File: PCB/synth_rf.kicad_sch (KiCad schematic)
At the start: 60 parts, among them J2 SMA CLK0, J3 SMA CLK1, J4 SMA CLK2, U2 Si5351A-B-GT, X1 25MHz TCXO

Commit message: Schematic: US resistor symbols, decoupling caps at their ICs, drop finalized VERIFY notes
- Device:R_Small -> Device:R_Small_US on all 30 resistors (same pin geometry; refs/values/fields/footprints/LCSC unchanged)
- Move label-connected decoupling caps next to their ICs: C10/C11 + C12/C13 at U3, C15/C16 at U4, C4 at U2
- Add PCB placement notes by U1, U5, U3, U4, U2/X1 and DS1 (pins from netlist)
- Remove VERIFY note lines and VERIFY fields for items Jason finalized:
  J1 D1 C10 U3 FB2 DS1 C17 SW1 X1 C100 R101 L1 C105
- Netlist identical to 4963a6d; ERC 0 errors
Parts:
- C100: VERIFY DC-block LF corner ~32 kHz into 50 ohm (PLAN Q6). -> (none)
- C105: VERIFY 9.1p only +/-0.25pF in stock (C513588); 24p +/-2% stock thi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 -> (none)
- L1: VERIFY LQW2UAS stock 0.9-3.3k/part; buy ahead. 150n uses +/-1% C20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 -> (none)
- R100, R120, R121, R140, R141, R27, R28, R5, R6: symbol Device:R_Small -> Device:R_Small_US
- R101: symbol Device:R_Small -> Device:R_Small_US; VERIFY DNP shunt ~120 ohm back-match of ~85 ohm source (datasheet 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 -> (none)
- X1: VERIFY TCXO stock thin (718); buy before ordering. -> (none)
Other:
- note added: "PCB: C4 100n at U2 pins 1 (VDD) + 7 (VDDO), tight loop to pin 8 (GND); GND via at cap pad. C5 100n at X1 pin 4 (VDD)."
- note added: "VERIFY (unconfirmed items on this sheet): - R27: I2C pull-up value not fixed (PLAN 2.2-4.7k); no LCSC chosen. On +3V3D: ATtiny, Si5351, CP2102N and OLED all at 3.3 V, so I2C levels match. - R28: as R27 - R100: 0603 0R series (Jason decision); LCSC code not in PLAN (C17477 is 0805). - J2: Footprint is a placeholder; check BWSMA-KE-P001 launch geometry and 1.6 mm edge fit. - R120: see R100 - R121: 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"
- note removed: "VERIFY (unconfirmed items on this sheet): - X1: TCXO stock thin (718); buy before ordering. - R27: I2C pull-up value not fixed (PLAN 2.2-4.7k); no LCSC chosen. On +3V3D: ATtiny, Si5351, CP2102N and OLED all at 3.3 V, so I2C levels match. - R28: as R27 - R100: 0603 0R series (Jason decision); LCSC code not in PLAN (C17477 is 0805). - C100: DC-block LF corner ~32 kHz into 50 ohm (PLAN Q6). - R101: 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"
- moved on the sheet: C4
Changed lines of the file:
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@@
 		(comment 1 "Draft schematic, not reviewed. See VERIFY notes.")
 	)
-	(text "VERIFY (unconfirmed items on this sheet):\n- X1: TCXO stock thin (718); buy before ordering.\n- R27: I2C pull-up value not fixed (PLAN 2.2-4.7k); no LCSC chosen. On +3V3D: ATtiny, Si5351, CP2102N and OLED all at\n   3.3 V, so I2C levels match.\n- R28: as R27\n- R100: 0603 0R series (Jason decision); LCSC code not in PLAN (C17477 is 0805).\n- C100: DC-block LF corner ~32 kHz into 50 ohm (PLAN Q6).\n- R101: DNP shunt ~120 ohm back-match of ~85 ohm source (datasheet Zo); part/LCSC not chosen; verify return loss esp.\n   >100 MHz.\n- L1: LQW2UAS stock 0.9-3.3k/part; buy ahead. 150n uses +/-1% C2044861 (C2043109 is +/-5%).\n- C105: 9.1p only +/-0.25pF in stock (C513588); 24p +/-2% stock thin (C2857979, ~950).\n- J2: Footprint is a placeholder; check BWSMA-KE-P001 launch geometry and 1.6 mm edge fit.\n- R120: see R100\n- R121: see R100\n- J3: see J2\n- R140: see R100\n- R141: see R100\n- J4: see J2"
+	(text "VERIFY (unconfirmed items on this sheet):\n- R27: I2C pull-up value not fixed (PLAN 2.2-4.7k); no LCSC chosen. On +3V3D: ATtiny, Si5351, CP2102N and OLED all at\n   3.3 V, so I2C levels match.\n- R28: as R27\n- R100: 0603 0R series (Jason decision); LCSC code not in PLAN (C17477 is 0805).\n- J2: Footprint is a placeholder; check BWSMA-KE-P001 launch geometry and 1.6 mm edge fit.\n- R120: see R100\n- R121: see R100\n- J3: see J2\n- R140: see R100\n- R141: see R100\n- J4: see J2"
 		(exclude_from_sim no)
 		(at 290 40 0)
@@
 		)
 	)
+	(text "PCB: C4 100n at U2 pins 1 (VDD) + 7 (VDDO), tight loop\nto pin 8 (GND); GND via at cap pad. C5 100n at X1 pin 4 (VDD)."
+		(exclude_from_sim no)
+		(at 162.56 62.23 0)
+		(effects
+			(font
+				(size 1.27 1.27)
+			)
+			(justify left top)
+		)
+	)
 	(junction
 		(at 165.1 264.16)
@@
 			)
 		)
-		(property "VERIFY" "LQW2UAS stock 0.9-3.3k/part; buy ahead. 150n uses +/-1% C2044861 (C2043109 is +/-5%)."
-			(at 121.92 172.72 0)
-			(hide yes)
-			(show_name no)
-			(do_not_autoplace no)
-			(effects
-				(font
-					(size 1.27 1.27)
-				)
-			)
-		)
 		(pin "1"
 		)
@@
 	)
 	(symbol
-		(lib_id "Device:R_Small")
+		(lib_id "Device:R_Small_US")
 		(at 139.7 129.54 0)
 		(unit 1)
@@
 	(symbol
 		(lib_id "Device:C_Small")
-		(at 165.1 59.69 0)
+		(at 154.94 76.2 0)
 		(unit 1)
 		(body_style 1)
@@
 		(dnp no)
 		(property "Reference" "C4"
-			(at 166.9 59.09 0)
+			(at 156.74 75.6 0)
 			(show_name no)
 			(do_not_autoplace no)
@@
 		)
 		(property "Value" "100n"
-			(at 166.9 61.29 0)
+			(at 156.74 77.8 0)
 			(show_name no)
 			(do_not_autoplace no)
@@
 		)
 		(property "Footprint" "Capacitor_SMD:C_0805_2012Metric"
-			(at 165.1 59.69 0)
+			(at 154.94 76.2 0)
 			(hide yes)
 			(show_name no)
@@
 		)
 		(property "Datasheet" ""
-			(at 165.1 59.69 0)
+			(at 154.94 76.2 0)
 			(hide yes)
 			(show_name no)
@@
 		)
 		(property "Description" "Unpolarized capacitor, small symbol"
-			(at 165.1 59.69 0)
+			(at 154.94 76.2 0)
 			(hide yes)
 			(show_name no)
@@
 		)
 		(property "LCSC" "C49678"
-			(at 165.1 59.69 0)
+			(at 154.94 76.2 0)
 			(hide yes)
 			(show_name no)
@@
 		)
 		(property "MPN" "CC0805KRX7R9BB104"
-			(at 165.1 59.69 0)
+			(at 154.94 76.2 0)
 			(hide yes)
 			(show_name no)
@@
 		)
 		(property "Manufacturer" "YAGEO"
-			(at 165.1 59.69 0)
+			(at 154.94 76.2 0)
 			(hide yes)
 			(show_name no)
@@
 	)
 	(symbol
-		(lib_id "Device:R_Small")
+		(lib_id "Device:R_Small_US")
 		(at 40.64 172.72 90)
 		(unit 1)
@@
 	)
 	(symbol
-		(lib_id "Device:R_Small")
+		(lib_id "Device:R_Small_US")
 		(at 40.64 264.16 90)
 		(unit 1)
@@
 			)
 		)
-		(property "VERIFY" "9.1p only +/-0.25pF in stock (C513588); 24p +/-2% stock thin (C2857979, ~950)."
-			(at 121.92 165.1 0)
-			(hide yes)
-			(show_name no)
-			(do_not_autoplace no)
-			(effects
-				(font
-					(size 1.27 1.27)
-				)
-			)
-		)
 		(pin "1"
 		)
@@
 			)
 		)
-		(property "VERIFY" "DC-block LF corner ~32 kHz into 50 ohm (PLAN Q6)."
-			(at 50.8 172.72 0)
-			(hide yes)
-			(show_name no)
-			(do_not_autoplace no)
-			(effects
-				(font
-					(size 1.27 1.27)
-				)
-			)
-		)
 		(pin "1"
 		)
@@
 	)
 	(symbol
-		(lib_id "Device:R_Small")
+		(lib_id "Device:R_Small_US")
 		(at 40.64 218.44 90)
 		(unit 1)
@@
 	)
 	(symbol
-		(lib_id "Device:R_Small")
+		(lib_id "Device:R_Small_US")
 		(at 60.96 177.8 0)
 		(unit 1)
@@
 			)
 		)
-		(property "VERIFY" "DNP shunt ~120 ohm back-match of ~85 ohm source (datasheet Zo); part/LCSC not chosen; verify return loss esp. >100 MHz."
-			(at 60.96 177.8 0)
-			(hide yes)
-			(show_name no)
-			(do_not_autoplace no)
-			(effects
-				(font
-					(size 1.27 1.27)
-				)
-			)
-		)
 		(pin "1"
 		)
@@
 	)
 	(symbol
-		(lib_id "Device:R_Small")
+		(lib_id "Device:R_Small_US")
 		(at 59.69 67.31 0)
 		(unit 1)
@@
 	)
 	(symbol
-		(lib_id "Device:R_Small")
+		(lib_id "Device:R_Small_US")
 		(at 60.96 223.52 0)
 		(unit 1)
@@
 			)
 		)
-		(property "VERIFY" "TCXO stock thin (718); buy before ordering."
-			(at 59.69 87.63 0)
-			(hide yes)
-			(show_name no)
-			(do_not_autoplace no)
-			(effects
-				(font
-					(size 1.27 1.27)
-				)
-			)
-		)
 		(pin "1"
 		)
@@
 	)
 	(symbol
-		(lib_id "Device:R_Small")
+		(lib_id "Device:R_Small_US")
 		(at 44.45 74.93 0)
 		(unit 1)
@@
 	)
 	(symbol
-		(lib_id "Device:R_Small")
+		(lib_id "Device:R_Small_US")
 		(at 100.33 129.54 0)
 		(unit 1)
@@
 	(symbol
 		(lib_id "power:GND")
-		(at 165.1 62.23 0)
+		(at 154.94 78.74 0)
 		(unit 1)
 		(body_style 1)
@@
 		(dnp no)
 		(property "Reference" "#PWR087"
-			(at 165.1 62.23 0)
+			(at 154.94 78.74 0)
 			(hide yes)
 			(show_name no)
@@
 		)
 		(property "Value" "GND"
-			(at 165.1 66.04 0)
+			(at 154.94 82.55 0)
 			(show_name no)
 			(do_not_autoplace no)
@@
 		)
 		(property "Footprint" ""
-			(at 165.1 62.23 0)
+			(at 154.94 78.74 0)
 			(hide yes)
 			(show_name no)
@@
 		)
 		(property "Datasheet" ""
-			(at 165.1 62.23 0)
+			(at 154.94 78.74 0)
 			(hide yes)
 			(show_name no)
@@
 		)
 		(property "Description" ""
-			(at 165.1 62.23 0)
+			(at 154.94 78.74 0)
 			(show_name no)
 			(do_not_autoplace no)
@@
 	)
 	(symbol
-		(lib_id "Device:R_Small")
+		(lib_id "Device:R_Small_US")
 		(at 60.96 269.24 0)
 		(unit 1)
@@
 	(symbol
 		(lib_id "power:+3V3")
-		(at 165.1 57.15 0)
+		(at 154.94 73.66 0)
 		(unit 1)
 		(body_style 1)
@@
 		(dnp no)
 		(property "Reference" "#PWR086"
-			(at 165.1 57.15 0)
+			(at 154.94 73.66 0)
 			(hide yes)
 			(show_name no)
@@
 		)
 		(property "Value" "+3V3_CLK"
-			(at 165.1 53.34 0)
+			(at 154.94 69.85 0)
 			(show_name no)
 			(do_not_autoplace no)
@@
 		)
 		(property "Footprint" ""
-			(at 165.1 57.15 0)
+			(at 154.94 73.66 0)
 			(hide yes)
 			(show_name no)
@@
 		)
 		(property "Datasheet" ""
-			(at 165.1 57.15 0)
+			(at 154.94 73.66 0)
 			(hide yes)
 			(show_name no)
@@
 		)
 		(property "Description" ""
-			(at 165.1 57.15 0)
+			(at 154.94 73.66 0)
 			(show_name no)
 			(do_not_autoplace no)

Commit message: Resolve VERIFY directives: R9 to VIO, R29 on PB4, OLED bulk, SMD UPDI parts, 4.7k I2C, 0805 0R, Etherkit SMA footprint
- R9 /RST pull-up moved from +5V to CP_VDD (CP2102N DS 2.1, Table 3.10)
- New R29 1k (C21190) between C14 and PB4 to limit DTR-rise injection current (ATtiny3226 DS Table 33-1)
- C24 fitted 22u 1206 (C12891); C22/C23 kept 2x4.7u
- R13 0603 C23179, D4 1N5711W SOD-123 C154843, J5 1x4 pin header C124378
- R27/R28 4.7k C17673; R100/R120/R140 0805 0R C17477; R101/R121/R141 LCSC C17437 (DNP)
- J2-J4 footprint EtherkitKicadLibrary:SMA-ENDLAUNCH
- H1-H4 and solder jumpers excluded from BOM
- Finalized VERIFY notes removed from sheets; VERIFY.md items ticked with KiCad EE notes
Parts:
- J2, J3, J4: footprint Connector_Coaxial:SMA_Samtec_SMA-J-P-H-ST-EM1_EdgeMount -> EtherkitKicadLibrary:SMA-ENDLAUNCH
- JP102, JP103, JP104, JP122, JP123, JP124, JP142, JP143, JP144: now left out of the parts list
- R100, R120, R140: footprint Resistor_SMD:R_0603_1608Metric -> Resistor_SMD:R_0805_2012Metric; LCSC (none) -> C17477; MPN (none) -> 0805W8F0000T5E; Manufacturer (none) -> UNI-ROYAL
- R101, R121, R141: LCSC (none) -> C17437; MPN (none) -> 0805W8F1200T5E; Manufacturer (none) -> UNI-ROYAL
- R27, R28: value VERIFY 2.2k-4.7k -> 4.7k; LCSC (none) -> C17673; MPN (none) -> 0805W8F4701T5E; Manufacturer (none) -> UNI-ROYAL
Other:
- note removed: "VERIFY (unconfirmed items on this sheet): - R27: I2C pull-up value not fixed (PLAN 2.2-4.7k); no LCSC chosen. On +3V3D: ATtiny, Si5351, CP2102N and OLED all at 3.3 V, so I2C levels match. - R28: as R27 - R100: 0603 0R series (Jason decision); LCSC code not in PLAN (C17477 is 0805). - J2: Footprint is a placeholder; check BWSMA-KE-P001 launch geometry and 1.6 mm edge fit. - R120: see R100 - R121: 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"

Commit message: Pre-layout: project-local Etherkit libs (ERC 0/0), DS1/J2-J4/X1 fit review, title block, clear finalized VERIFY fields, LPF closed
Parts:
- J2: VERIFY Footprint is a placeholder; check BWSMA-KE-P001 launch geom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 -> (none)
- J3, J4: VERIFY see J2 -> (none)
- R100: VERIFY 0603 0R series (Jason decision); LCSC code not in PLAN (C17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 -> (none)
- R120, R121, R140, R141: VERIFY see R100 -> (none)
- R27: VERIFY I2C pull-up value not fixed (PLAN 2.2-4.7k); no LCSC chosen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 -> (none)
- R28: VERIFY as R27 -> (none)
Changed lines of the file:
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@@
 		(rev "A")
 		(company "Etherkit / NT7S")
-		(comment 1 "Draft schematic, not reviewed. See VERIFY notes.")
+		(comment 1 "Draft schematic, not reviewed. Open items: docs/VERIFY.md")
 	)
 	(text "CLK0 output chain (J2)"
@@
 			)
 		)
-		(property "VERIFY" "as R27"
-			(at 139.7 129.54 0)
-			(hide yes)
-			(show_name no)
-			(do_not_autoplace no)
-			(effects
-				(font
-					(size 1.27 1.27)
-				)
-			)
-		)
 		(property "LCSC" "C17673"
 			(at 139.7 129.54 0)
@@
 			)
 		)
-		(property "VERIFY" "Footprint is a placeholder; check BWSMA-KE-P001 launch geometry and 1.6 mm edge fit."
-			(at 203.2 172.72 0)
-			(hide yes)
-			(show_name no)
-			(do_not_autoplace no)
-			(effects
-				(font
-					(size 1.27 1.27)
-				)
-			)
-		)
 		(pin "1"
 		)
@@
 			)
 		)
-		(property "VERIFY" "0603 0R series (Jason decision); LCSC code not in PLAN (C17477 is 0805)."
-			(at 40.64 172.72 0)
-			(hide yes)
-			(show_name no)
-			(do_not_autoplace no)
-			(effects
-				(font
-					(size 1.27 1.27)
-				)
-			)
-		)
 		(property "MPN" "0805W8F0000T5E"
 			(at 40.64 172.72 0)
@@
 			)
 		)
-		(property "VERIFY" "see R100"
-			(at 40.64 264.16 0)
-			(hide yes)
-			(show_name no)
-			(do_not_autoplace no)
-			(effects
-				(font
-					(size 1.27 1.27)
-				)
-			)
-		)
 		(property "MPN" "0805W8F0000T5E"
 			(at 40.64 264.16 0)
@@
 			)
 		)
-		(property "VERIFY" "see J2"
-			(at 203.2 264.16 0)
-			(hide yes)
-			(show_name no)
-			(do_not_autoplace no)
-			(effects
-				(font
-					(size 1.27 1.27)
-				)
-			)
-		)
 		(pin "1"
 		)
@@
 			)
 		)
-		(property "VERIFY" "see R100"
-			(at 40.64 218.44 0)
-			(hide yes)
-			(show_name no)
-			(do_not_autoplace no)
-			(effects
-				(font
-					(size 1.27 1.27)
-				)
-			)
-		)
 		(property "MPN" "0805W8F0000T5E"
 			(at 40.64 218.44 0)
@@
 			)
 		)
-		(property "VERIFY" "see R100"
-			(at 60.96 223.52 0)
-			(hide yes)
-			(show_name no)
-			(do_not_autoplace no)
-			(effects
-				(font
-					(size 1.27 1.27)
-				)
-			)
-		)
 		(property "LCSC" "C17437"
 			(at 60.96 223.52 0)
@@
 			)
 		)
-		(property "VERIFY" "see J2"
-			(at 203.2 218.44 0)
-			(hide yes)
-			(show_name no)
-			(do_not_autoplace no)
-			(effects
-				(font
-					(size 1.27 1.27)
-				)
-			)
-		)
 		(pin "1"
 		)
@@
 			)
 		)
-		(property "VERIFY" "I2C pull-up value not fixed (PLAN 2.2-4.7k); no LCSC chosen. On +3V3D: ATtiny, Si5351, CP2102N and OLED all at 3.3 V, so I2C levels match."
-			(at 100.33 129.54 0)
-			(hide yes)
-			(show_name no)
-			(do_not_autoplace no)
-			(effects
-				(font
-					(size 1.27 1.27)
-				)
-			)
-		)
 		(property "LCSC" "C17673"
 			(at 100.33 129.54 0)
@@
 			(at 60.96 269.24 0)
 			(hide yes)
-			(show_name no)
-			(do_not_autoplace no)
-			(effects
-				(font
-					(size 1.27 1.27)
-				)
-			)
-		)
-		(property "VERIFY" "see R100"
-			(at 60.96 269.24 0)
-			(hide yes)

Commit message: J2-J4 SMA: DNP, supplied in kit, user-soldered; off BOM/pos, LCSC cleared, MPN kept; VERIFY + regen docs
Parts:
- J2, J3, J4: LCSC C496550 -> (none); now not fitted; now left out of the parts list
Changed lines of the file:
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@@
 		(body_style 1)
 		(exclude_from_sim no)
-		(in_bom yes)
+		(in_bom no)
 		(on_board yes)
-		(in_pos_files yes)
-		(dnp no)
+		(in_pos_files no)
+		(dnp yes)
 		(property "Reference" "J2"
 			(at 203.454 169.672 0)
@@
 			)
 		)
-		(property "Description" "coaxial connector (BNC, SMA, SMB, SMC, Cinch/RCA, LEMO, ...)"
+		(property "Description" "SMA end-launch jack, edge mount. DNP, supplied in kit, user-soldered."
 			(at 203.2 172.72 0)
 			(hide yes)
@@
 			)
 		)
-		(property "LCSC" "C496550"
+		(property "LCSC" ""
 			(at 203.2 172.72 0)
 			(hide yes)
@@
 		(body_style 1)
 		(exclude_from_sim no)
-		(in_bom yes)
+		(in_bom no)
 		(on_board yes)
-		(in_pos_files yes)
-		(dnp no)
+		(in_pos_files no)
+		(dnp yes)
 		(property "Reference" "J4"
 			(at 203.454 261.112 0)
@@
 			)
 		)
-		(property "Description" "coaxial connector (BNC, SMA, SMB, SMC, Cinch/RCA, LEMO, ...)"
+		(property "Description" "SMA end-launch jack, edge mount. DNP, supplied in kit, user-soldered."
 			(at 203.2 264.16 0)
 			(hide yes)
@@
 			)
 		)
-		(property "LCSC" "C496550"
+		(property "LCSC" ""
 			(at 203.2 264.16 0)
 			(hide yes)
@@
 		(body_style 1)
 		(exclude_from_sim no)
-		(in_bom yes)
+		(in_bom no)
 		(on_board yes)
-		(in_pos_files yes)
-		(dnp no)
+		(in_pos_files no)
+		(dnp yes)
 		(property "Reference" "J3"
 			(at 203.454 215.392 0)
@@
 			)
 		)
-		(property "Description" "coaxial connector (BNC, SMA, SMB, SMC, Cinch/RCA, LEMO, ...)"
+		(property "Description" "SMA end-launch jack, edge mount. DNP, supplied in kit, user-soldered."
 			(at 203.2 218.44 0)
 			(hide yes)
@@
 			)
 		)
-		(property "LCSC" "C496550"
+		(property "LCSC" ""
 			(at 203.2 218.44 0)
 			(hide yes)

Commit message: Bypass: split each bypass jumper into two NO jumpers (JP104+JP105, JP124+JP125, JP144+JP145) with CLKn_BYP lane net, isolating the lane at both ends; regen docs
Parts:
- added JP105, JP125, JP145: NO, Jumper:SolderJumper-2_P1.3mm_Open_RoundedPad1.0x1.5mm, symbol Jumper:SolderJumper_2_Open
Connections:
- net at J2.1 (In), JP103.2 (B): now also JP105.2 (B); no longer JP104.2 (B)
- net at J4.1 (In), JP143.2 (B): now also JP145.2 (B); no longer JP144.2 (B)
- net at J3.1 (In), JP123.2 (B): now also JP125.2 (B); no longer JP124.2 (B)
- new net CLK0_BYP: JP104.2 (B), JP105.1 (A)
- new net CLK1_BYP: JP124.2 (B), JP125.1 (A)
- new net CLK2_BYP: JP144.2 (B), JP145.1 (A)

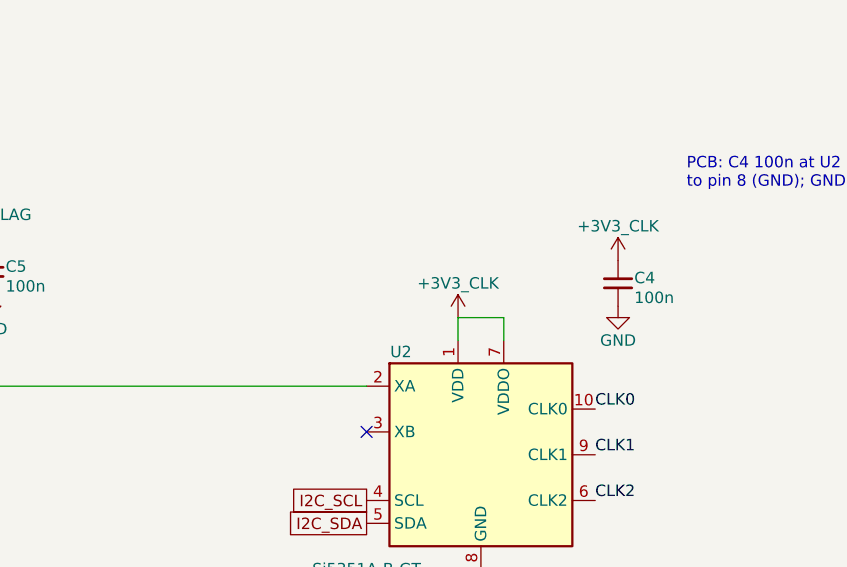
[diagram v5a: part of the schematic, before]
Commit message: Sync schematic from rev-a-schematic (24008ef): C26/C27/C28 U2 decoupling, 0402 CLK series Rs, RF50 incl. CLK*_BYP; regen docs
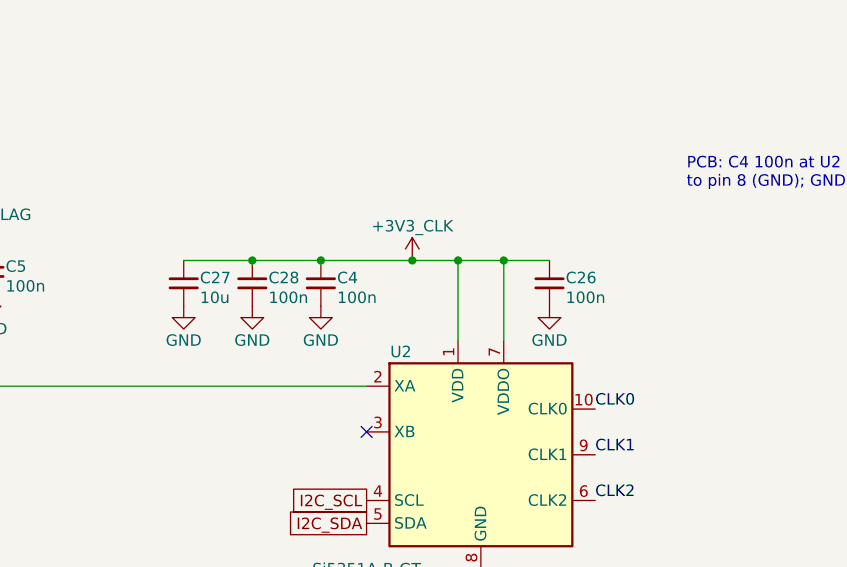
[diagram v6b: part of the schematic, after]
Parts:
- added C26: 100n, Capacitor_SMD:C_0402_1005Metric, symbol Device:C_Small
- added C27: 10u, Capacitor_SMD:C_0805_2012Metric, symbol Device:C_Small
- added C28: 100n, Capacitor_SMD:C_0805_2012Metric, symbol Device:C_Small
- R100, R120, R140: footprint Resistor_SMD:R_0805_2012Metric -> Resistor_SMD:R_0402_1005Metric; LCSC C17477 -> C17168; MPN 0805W8F0000T5E -> 0402WGF0000TCE
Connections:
- net +3V3_CLK: now also C26.1, C27.1, C28.1
- net GND: now also C26.2, C27.2, C28.2
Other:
- moved on the sheet: C4
